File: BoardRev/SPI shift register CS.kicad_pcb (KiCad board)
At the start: 2 copper layers, 114.3 x 29.2 mm, 22 parts, among them J1 CONN_06, J10 CONN_07, J2 CONN_06, J3 CONN_06, J4 CONN_06, J5 CONN_06, J6 CONN_06, J7 CONN_06, J8 CONN_06, J9 CONN_07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

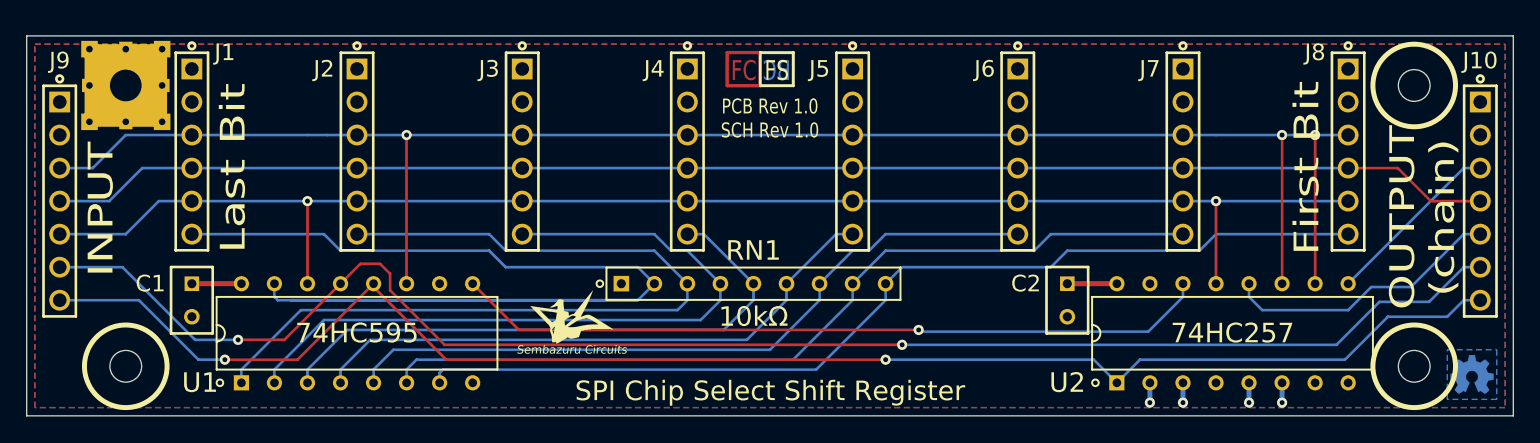
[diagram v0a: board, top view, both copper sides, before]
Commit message: v1.0.1 Add labels to output connectors
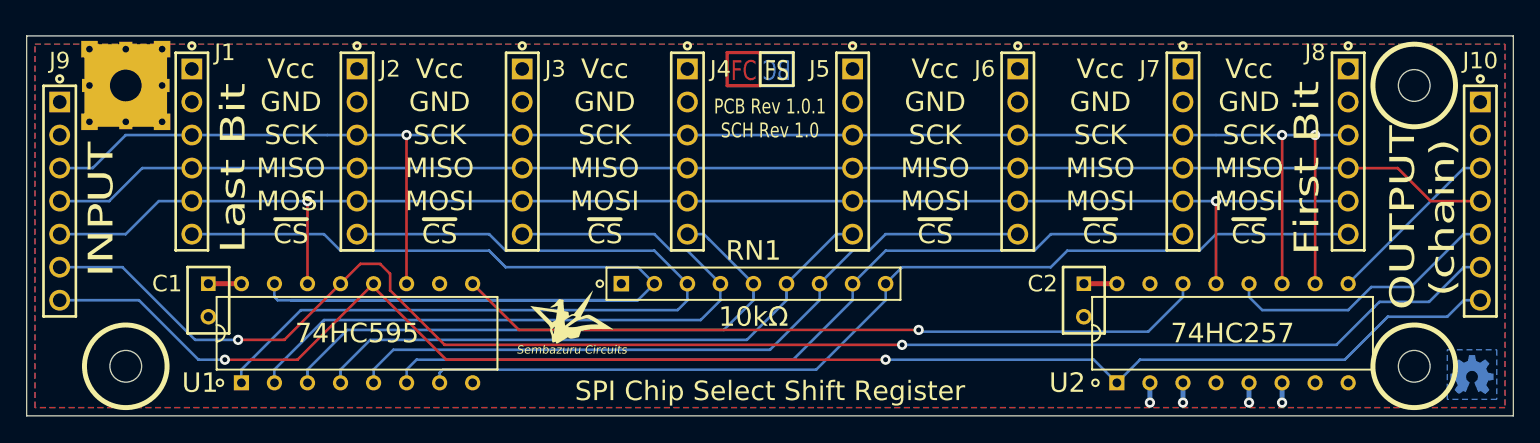
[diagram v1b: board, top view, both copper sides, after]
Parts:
- moved C1 1.27 mm to (90.2, 96.5)
- moved C2 1.27 mm to (157.5, 96.5)
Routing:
- net VCC: track 7.62 -> 5.08 mm
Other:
- board text added: "GND"
- board text added: "MISO"
- board text added: "MOSI"
- board text added: "PCB Rev 1.0.1 SCH Rev 1.0"
- board text added: "SCK"
- board text added: "Vcc"
- board text added: "~CS"
- board text removed: "PCB Rev 1.0 SCH Rev 1.0"
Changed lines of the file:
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@@
     (area 52.654287 68.35 195.179648 150.02)
     (thickness 1.6)
-    (drawings 94)
+    (drawings 130)
     (tracks 195)
     (zones 0)
@@
   (title_block
     (title "SPI Shift Register 8 Device Select")
-    (date "Wednesday, December 31, 2014")
-    (rev 1.0)
+    (date 2015-09-04)
+    (rev 1.0.1)
     (company "Sembazuru Circuits")
-    (comment 4 "v1.0 - First iteration")
+    (comment 3 "v1.0.1 - Add labeling for output pinouts & shift bypass caps.")
+    (comment 4 "v1.0 - First iteration.")
   )
   (layers
@@
   )
   (module "ipc-7251TH Standard:CAPRR254W51L508T318H660P" (layer F.Cu)
-    (at 88.9 96.52 270)
+    (at 90.17 96.52 270)
     (descr footprints_doc/CAPRR254W51L508T318H660P.pdf)
     (tags CAPRR254W51L508T318H660)
@@
   )
   (module "ipc-7251TH Standard:CAPRR254W51L508T318H660P" (layer F.Cu)
-    (at 156.21 96.52 270)
+    (at 157.48 96.52 270)
     (descr footprints_doc/CAPRR254W51L508T318H660P.pdf)
     (tags CAPRR254W51L508T318H660)
@@
     (descr "Header Vertical 6Pin 0.100” Pitch 1X6 Fabrication Level P(Proportional)")
     (tags HDRV6W64P254_1X6_1524X254X1016)
-    (fp_text reference J2 (at -6.35 2.54 360) (layer F.SilkS)
+    (fp_text reference J2 (at -6.35 -2.54 360) (layer F.SilkS)
       (effects (font (size 1.27 1.27) (thickness 0.2032)))
     )
@@
     (descr "Header Vertical 6Pin 0.100” Pitch 1X6 Fabrication Level P(Proportional)")
     (tags HDRV6W64P254_1X6_1524X254X1016)
-    (fp_text reference J3 (at -6.35 2.54 360) (layer F.SilkS)
+    (fp_text reference J3 (at -6.35 -2.54 360) (layer F.SilkS)
       (effects (font (size 1.27 1.27) (thickness 0.2032)))
     )
@@
     (descr "Header Vertical 6Pin 0.100” Pitch 1X6 Fabrication Level P(Proportional)")
     (tags HDRV6W64P254_1X6_1524X254X1016)
-    (fp_text reference J4 (at -6.35 2.54 360) (layer F.SilkS)
+    (fp_text reference J4 (at -6.35 -2.54 360) (layer F.SilkS)
       (effects (font (size 1.27 1.27) (thickness 0.2032)))
     )
@@
     (fp_line (start -1.27 -1.27) (end -1.27 1.27) (layer B.SilkS) (width 0.2032))
   )
-  (gr_text "PCB Rev 1.0\nSCH Rev 1.0" (at 133.35 82.55) (layer F.SilkS)
+  (gr_text Vcc (at 158.75 78.74) (layer F.SilkS)
+    (effects (font (size 1.5 1.5) (thickness 0.3)))
+  )
+  (gr_text GND (at 158.75 81.28) (layer F.SilkS)
+    (effects (font (size 1.5 1.5) (thickness 0.3)))
+  )
+  (gr_text SCK (at 158.75 83.82) (layer F.SilkS)
+    (effects (font (size 1.5 1.5) (thickness 0.3)))
+  )
+  (gr_text MISO (at 158.75 86.36) (layer F.SilkS)
+    (effects (font (size 1.5 1.5) (thickness 0.3)))
+  )
+  (gr_text MOSI (at 158.75 88.9) (layer F.SilkS)
+    (effects (font (size 1.5 1.5) (thickness 0.3)))
+  )
+  (gr_text ~CS (at 158.75 91.44) (layer F.SilkS)
+    (effects (font (size 1.5 1.5) (thickness 0.3)))
+  )
+  (gr_text ~CS (at 107.95 91.44) (layer F.SilkS)
+    (effects (font (size 1.5 1.5) (thickness 0.3)))
+  )
+  (gr_text MOSI (at 107.95 88.9) (layer F.SilkS)
+    (effects (font (size 1.5 1.5) (thickness 0.3)))
+  )
+  (gr_text MISO (at 107.95 86.36) (layer F.SilkS)
+    (effects (font (size 1.5 1.5) (thickness 0.3)))
+  )
+  (gr_text SCK (at 107.95 83.82) (layer F.SilkS)
+    (effects (font (size 1.5 1.5) (thickness 0.3)))
+  )
+  (gr_text GND (at 107.95 81.28) (layer F.SilkS)
+    (effects (font (size 1.5 1.5) (thickness 0.3)))
+  )
+  (gr_text Vcc (at 107.95 78.74) (layer F.SilkS)
+    (effects (font (size 1.5 1.5) (thickness 0.3)))
+  )
+  (gr_text ~CS (at 96.52 91.44) (layer F.SilkS)
+    (effects (font (size 1.5 1.5) (thickness 0.3)))
+  )
+  (gr_text MOSI (at 96.52 88.9) (layer F.SilkS)
+    (effects (font (size 1.5 1.5) (thickness 0.3)))
+  )
+  (gr_text MISO (at 96.52 86.36) (layer F.SilkS)
+    (effects (font (size 1.5 1.5) (thickness 0.3)))
+  )
+  (gr_text SCK (at 96.52 83.82) (layer F.SilkS)
+    (effects (font (size 1.5 1.5) (thickness 0.3)))
+  )
+  (gr_text GND (at 96.52 81.28) (layer F.SilkS)
+    (effects (font (size 1.5 1.5) (thickness 0.3)))
+  )
+  (gr_text Vcc (at 96.52 78.74) (layer F.SilkS)
+    (effects (font (size 1.5 1.5) (thickness 0.3)))
+  )
+  (gr_text Vcc (at 120.65 78.74) (layer F.SilkS)
+    (effects (font (size 1.5 1.5) (thickness 0.3)))
+  )
+  (gr_text GND (at 120.65 81.28) (layer F.SilkS)
+    (effects (font (size 1.5 1.5) (thickness 0.3)))
+  )
+  (gr_text SCK (at 120.65 83.82) (layer F.SilkS)
+    (effects (font (size 1.5 1.5) (thickness 0.3)))
+  )
+  (gr_text MISO (at 120.65 86.36) (layer F.SilkS)
+    (effects (font (size 1.5 1.5) (thickness 0.3)))
+  )
+  (gr_text MOSI (at 120.65 88.9) (layer F.SilkS)
+    (effects (font (size 1.5 1.5) (thickness 0.3)))
+  )
+  (gr_text ~CS (at 120.65 91.44) (layer F.SilkS)
+    (effects (font (size 1.5 1.5) (thickness 0.3)))
+  )
+  (gr_text Vcc (at 170.18 78.74) (layer F.SilkS)
+    (effects (font (size 1.5 1.5) (thickness 0.3)))
+  )
+  (gr_text GND (at 170.18 81.28) (layer F.SilkS)
+    (effects (font (size 1.5 1.5) (thickness 0.3)))
+  )
+  (gr_text SCK (at 170.18 83.82) (layer F.SilkS)
+    (effects (font (size 1.5 1.5) (thickness 0.3)))
+  )
+  (gr_text MISO (at 170.18 86.36) (layer F.SilkS)
+    (effects (font (size 1.5 1.5) (thickness 0.3)))
+  )
+  (gr_text MOSI (at 170.18 88.9) (layer F.SilkS)
+    (effects (font (size 1.5 1.5) (thickness 0.3)))
+  )
+  (gr_text ~CS (at 170.18 91.44) (layer F.SilkS)
+    (effects (font (size 1.5 1.5) (thickness 0.3)))
+  )
+  (gr_text ~CS (at 146.05 91.44) (layer F.SilkS)
+    (effects (font (size 1.5 1.5) (thickness 0.3)))
+  )
+  (gr_text MOSI (at 146.05 88.9) (layer F.SilkS)
+    (effects (font (size 1.5 1.5) (thickness 0.3)))
+  )
+  (gr_text MISO (at 146.05 86.36) (layer F.SilkS)
+    (effects (font (size 1.5 1.5) (thickness 0.3)))
+  )
+  (gr_text SCK (at 146.05 83.82) (layer F.SilkS)
+    (effects (font (size 1.5 1.5) (thickness 0.3)))
+  )
+  (gr_text GND (at 146.05 81.28) (layer F.SilkS)
+    (effects (font (size 1.5 1.5) (thickness 0.3)))
+  )
+  (gr_text Vcc (at 146.05 78.74) (layer F.SilkS)
+    (effects (font (size 1.5 1.5) (thickness 0.3)))
+  )
+  (gr_text "PCB Rev 1.0.1\nSCH Rev 1.0" (at 133.35 82.55) (layer F.SilkS)
     (effects (font (size 1.143 0.889) (thickness 0.22225)))
   )
@@
   (gr_line (start 190.5 76.2) (end 190.5 105.41) (angle 90) (layer Edge.Cuts) (width 0.1))
   (gr_line (start 190.5 76.2) (end 76.2 76.2) (angle 90) (layer Edge.Cuts) (width 0.1))
-  (segment (start 88.9 95.25) (end 92.71 95.25) (width 0.381) (layer F.Cu) (net 1))
-  (segment (start 156.21 95.25) (end 160.02 95.25) (width 0.381) (layer F.Cu) (net 1))
+  (segment (start 90.17 95.25) (end 92.71 95.25) (width 0.381) (layer F.Cu) (net 1) (status 10))
+  (segment (start 157.48 95.25) (end 160.02 95.25) (width 0.381) (layer F.Cu) (net 1) (status 10))
   (via (at 162.56 104.394) (size 0.7874) (layers F.Cu B.Cu) (net 2))
   (segment (start 162.56 102.87) (end 162.56 104.394) (width 0.381) (layer B.Cu) (net 2))
